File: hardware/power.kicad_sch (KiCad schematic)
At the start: 48 parts, among them J3 Barrel_Jack_Switch, J6 5V EXT, Q10 RJK0355DSP, Q7 DMP3037LSS-13, Q8 2N7002, Q9 RJK0355DSP, U5 MIC2101

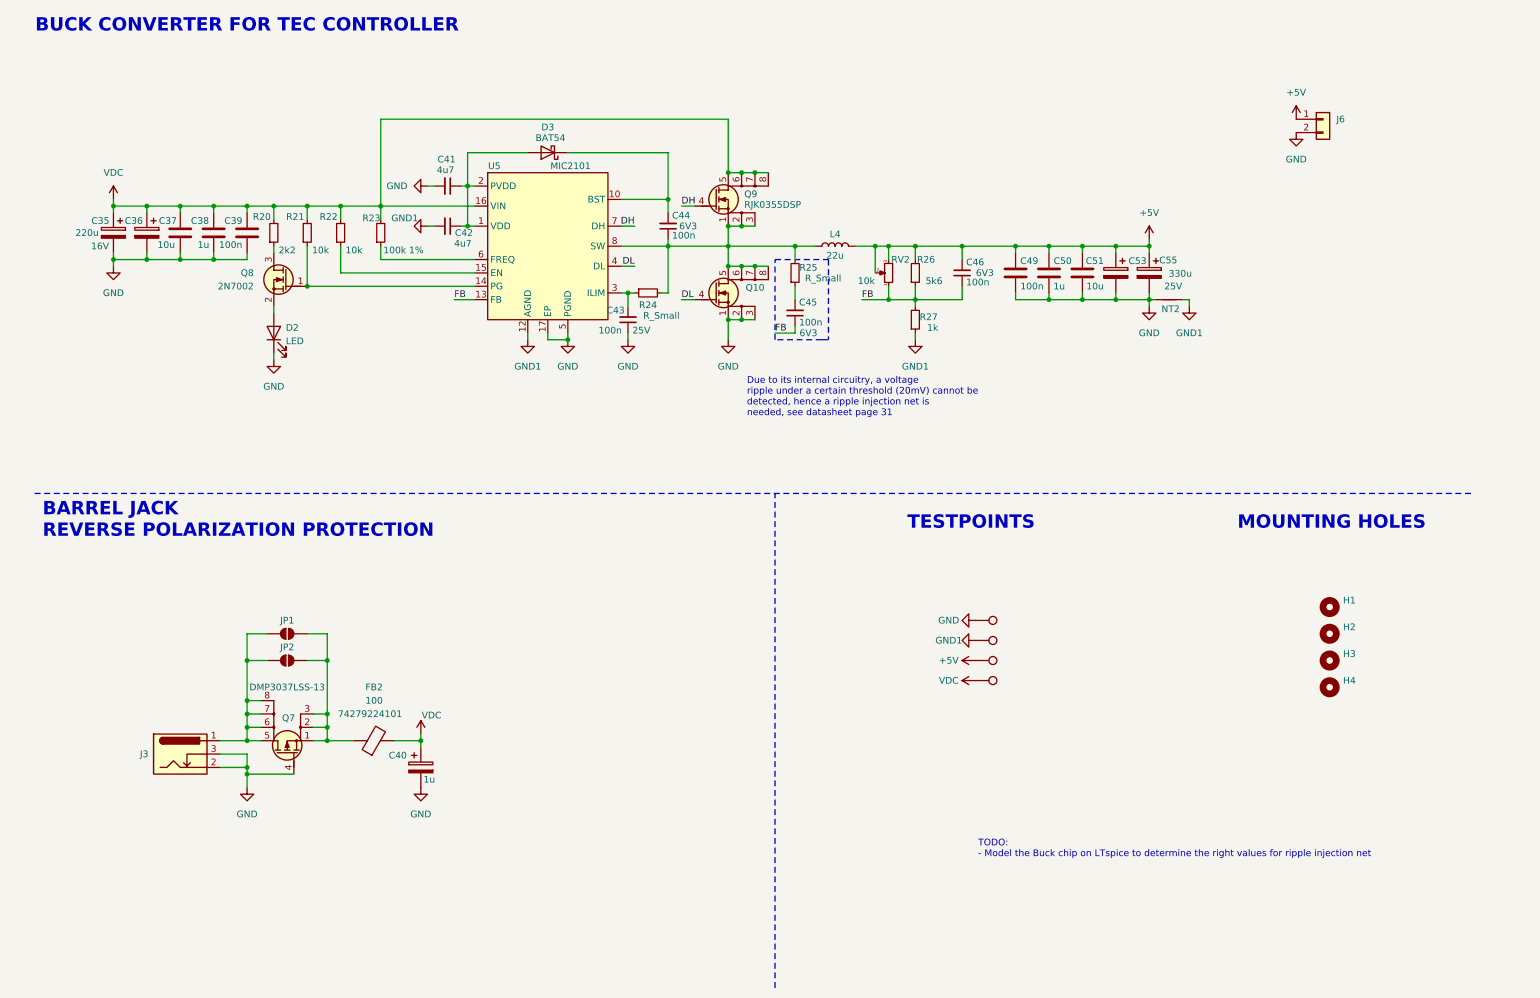
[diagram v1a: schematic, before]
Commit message: feat: syntethizing parser with output registers instead on using external reg, minor fixes to schematic and PCB
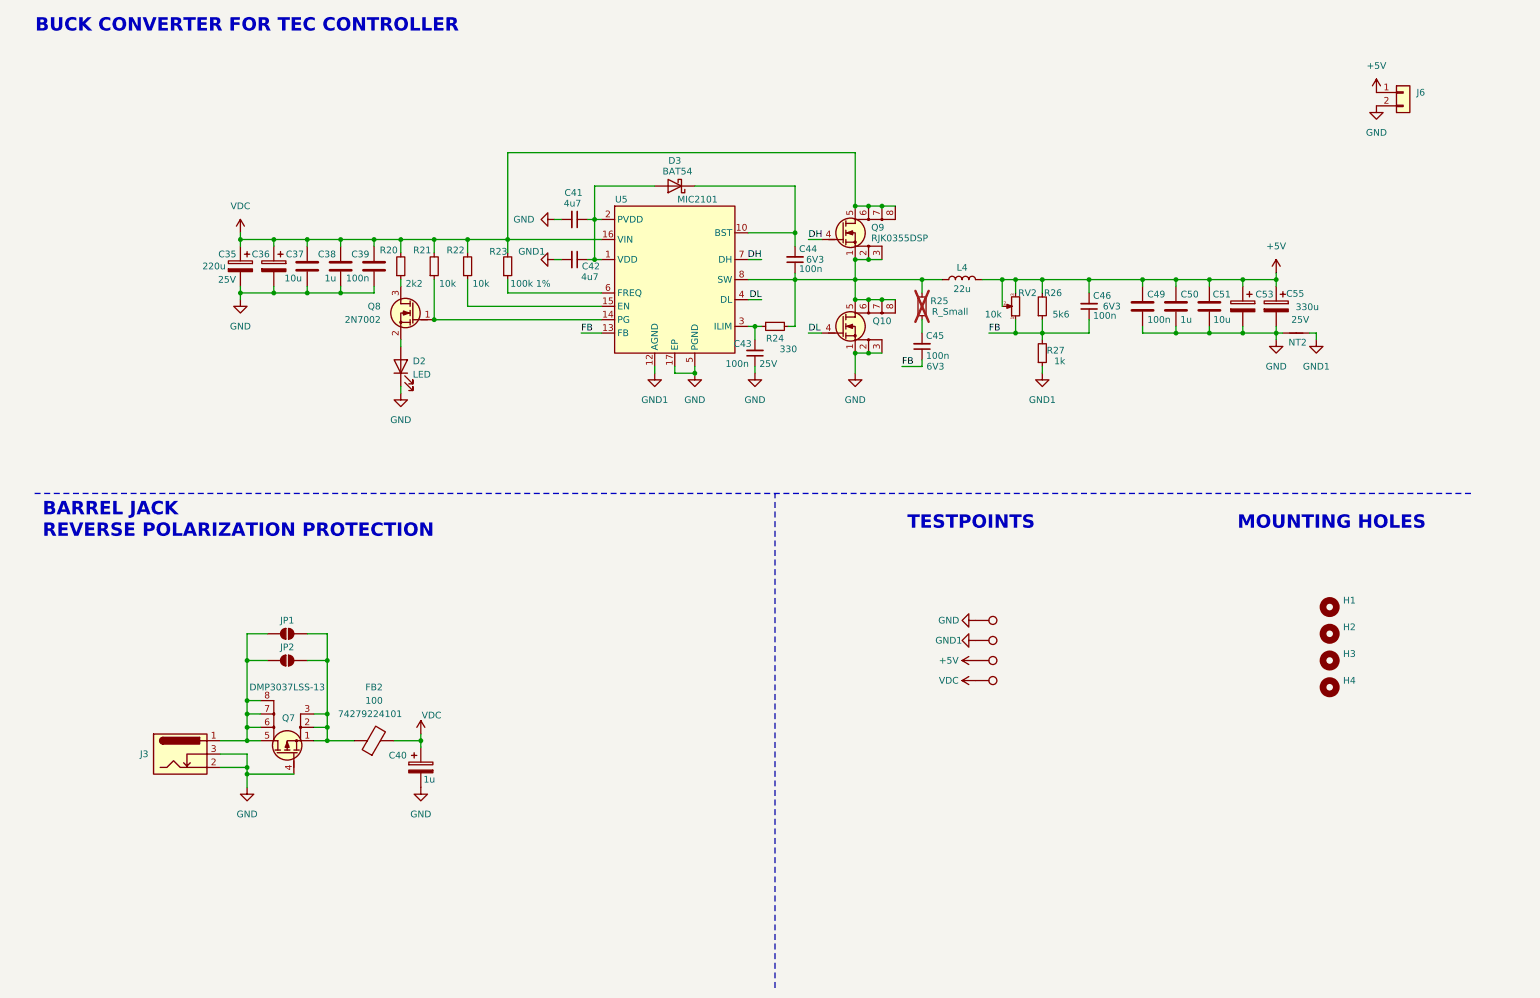
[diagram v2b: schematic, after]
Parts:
- C35: Voltage Rating 16V -> 25V
- R24: value R_Small -> 330
- R25: now not fitted
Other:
- note removed: "Due to its internal circuitry, a voltage ripple under a certain threshold (20mV) cannot be detected, hence a ripple injection net is needed, see datasheet page 31"
- note removed: "TODO: - Model the Buck chip on LTspice to determine the right values for ripple injection net"
- moved on the sheet: C35, C36, C37, C38, C39, C41, C42, C43, C44, C45, C46, C49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
